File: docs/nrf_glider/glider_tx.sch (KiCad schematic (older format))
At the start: 12 parts

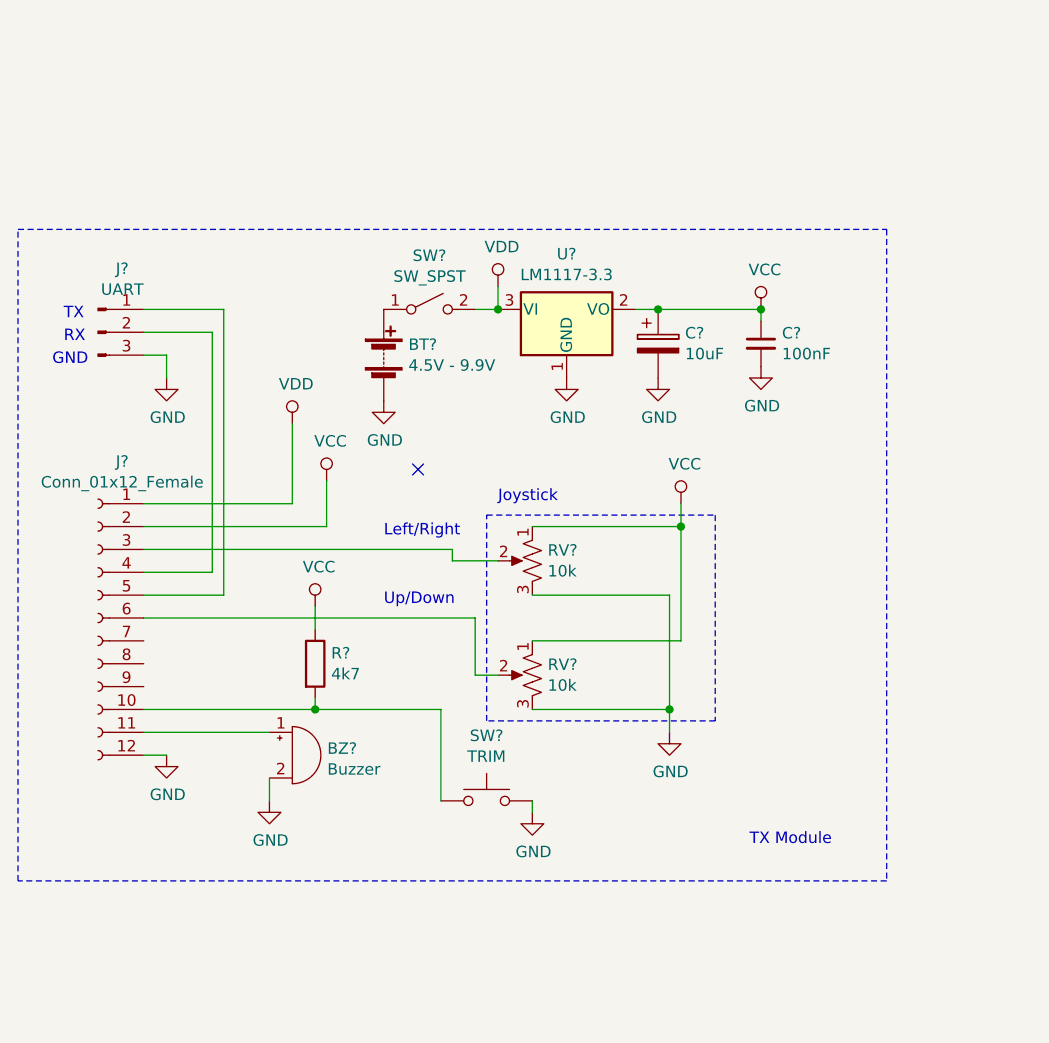
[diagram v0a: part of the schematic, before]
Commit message: added hierarchical sheets and labels
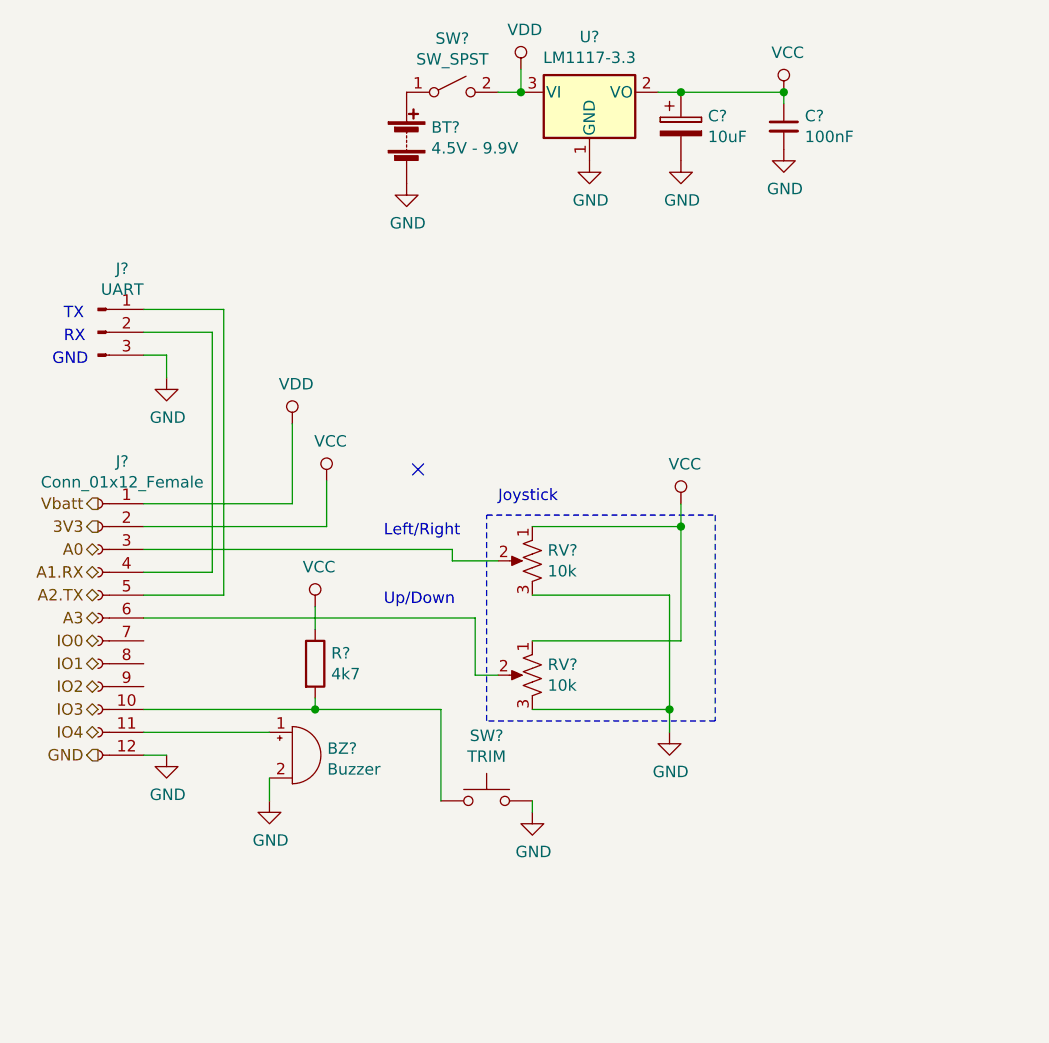
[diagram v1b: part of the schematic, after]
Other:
- note removed: "TX Module"
- moved on the sheet: BT?, C?, SW?, U?
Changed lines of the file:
@@
 $Descr A4 11693 8268
 encoding utf-8
-Sheet 1 4
+Sheet 3 5
 Title ""
 Date ""
@@
 L Regulator_Linear:LM1117-3.3 U?
 U 1 1 5BD2C866
-P 6200 2400
-F 0 "U?" H 6200 2642 50  0000 C CNN
-F 1 "LM1117-3.3" H 6200 2551 50  0000 C CNN
-F 2 "" H 6200 2400 50  0001 C CNN
-F 3 "http://www.ti.com/lit/ds/symlink/lm1117.pdf" H 6200 2400 50  0001 C CNN
-	1    6200 2400
+P 6300 1450
+F 0 "U?" H 6300 1692 50  0000 C CNN
+F 1 "LM1117-3.3" H 6300 1601 50  0000 C CNN
+F 2 "" H 6300 1450 50  0001 C CNN
+F 3 "http://www.ti.com/lit/ds/symlink/lm1117.pdf" H 6300 1450 50  0001 C CNN
+	1    6300 1450
 	1    0    0    -1
 $EndComp
@@
 L power:GND #PWR?
 U 1 1 5BD2C86D
-P 6200 2700
-F 0 "#PWR?" H 6200 2450 50  0001 C CNN
-F 1 "GND" H 6205 2527 50  0000 C CNN
-F 2 "" H 6200 2700 50  0001 C CNN
-F 3 "" H 6200 2700 50  0001 C CNN
-	1    6200 2700
+P 6300 1750
+F 0 "#PWR?" H 6300 1500 50  0001 C CNN
+F 1 "GND" H 6305 1577 50  0000 C CNN
+F 2 "" H 6300 1750 50  0001 C CNN
+F 3 "" H 6300 1750 50  0001 C CNN
+	1    6300 1750
 	1    0    0    -1
 $EndComp
@@
 L Device:Battery BT?
 U 1 1 5BD2C873
-P 5400 2600
-F 0 "BT?" H 5508 2646 50  0000 L CNN
-F 1 "4.5V - 9.9V" H 5508 2555 50  0000 L CNN
-F 2 "Connector_PinHeader_2.54mm:PinHeader_1x02_P2.54mm_Vertical" V 5400 2660 50  0001 C CNN
-F 3 "~" V 5400 2660 50  0001 C CNN
-	1    5400 2600
+P 5500 1650
+F 0 "BT?" H 5608 1696 50  0000 L CNN
+F 1 "4.5V - 9.9V" H 5608 1605 50  0000 L CNN
+F 2 "Connector_PinHeader_2.54mm:PinHeader_1x02_P2.54mm_Vertical" V 5500 1710 50  0001 C CNN
+F 3 "~" V 5500 1710 50  0001 C CNN
+	1    5500 1650
 	1    0    0    -1
 $EndComp
@@
 L power:GND #PWR?
 U 1 1 5BD2C87B
-P 5400 2800
-F 0 "#PWR?" H 5400 2550 50  0001 C CNN
-F 1 "GND" H 5405 2627 50  0000 C CNN
-F 2 "" H 5400 2800 50  0001 C CNN
-F 3 "" H 5400 2800 50  0001 C CNN
-	1    5400 2800
+P 5500 1850
+F 0 "#PWR?" H 5500 1600 50  0001 C CNN
+F 1 "GND" H 5505 1677 50  0000 C CNN
+F 2 "" H 5500 1850 50  0001 C CNN
+F 3 "" H 5500 1850 50  0001 C CNN
+	1    5500 1850
 	1    0    0    -1
 $EndComp
@@
 L power:VCC #PWR?
 U 1 1 5BD2C881
-P 7050 2400
-F 0 "#PWR?" H 7050 2250 50  0001 C CNN
-F 1 "VCC" H 7067 2573 50  0000 C CNN
-F 2 "" H 7050 2400 50  0001 C CNN
-F 3 "" H 7050 2400 50  0001 C CNN
-	1    7050 2400
+P 7150 1450
+F 0 "#PWR?" H 7150 1300 50  0001 C CNN
+F 1 "VCC" H 7167 1623 50  0000 C CNN
+F 2 "" H 7150 1450 50  0001 C CNN
+F 3 "" H 7150 1450 50  0001 C CNN
+	1    7150 1450
 	1    0    0    -1
 $EndComp
@@
 L Device:C_Small C?
 U 1 1 5BD2C887
-P 7050 2550
-F 0 "C?" H 7142 2596 50  0000 L CNN
-F 1 "100nF" H 7142 2505 50  0000 L CNN
-F 2 "Capacitor_THT:C_Disc_D5.0mm_W2.5mm_P5.00mm" H 7050 2550 50  0001 C CNN
-F 3 "~" H 7050 2550 50  0001 C CNN
-	1    7050 2550
+P 7150 1600
+F 0 "C?" H 7242 1646 50  0000 L CNN
+F 1 "100nF" H 7242 1555 50  0000 L CNN
+F 2 "Capacitor_THT:C_Disc_D5.0mm_W2.5mm_P5.00mm" H 7150 1600 50  0001 C CNN
+F 3 "~" H 7150 1600 50  0001 C CNN
+	1    7150 1600
 	1    0    0    -1
 $EndComp
@@
 L Device:CP C?
 U 1 1 5BD2C88E
-P 6600 2550
-F 0 "C?" H 6718 2596 50  0000 L CNN
-F 1 "10uF" H 6718 2505 50  0000 L CNN
-F 2 "Capacitor_THT:CP_Radial_D8.0mm_P2.50mm" H 6638 2400 50  0001 C CNN
-F 3 "~" H 6600 2550 50  0001 C CNN
-	1    6600 2550
+P 6700 1600
+F 0 "C?" H 6818 1646 50  0000 L CNN
+F 1 "10uF" H 6818 1555 50  0000 L CNN
+F 2 "Capacitor_THT:CP_Radial_D8.0mm_P2.50mm" H 6738 1450 50  0001 C CNN
+F 3 "~" H 6700 1600 50  0001 C CNN
+	1    6700 1600
 	1    0    0    -1
 $EndComp
@@
 L power:GND #PWR?
 U 1 1 5BD2C895
-P 6600 2700
-F 0 "#PWR?" H 6600 2450 50  0001 C CNN
-F 1 "GND" H 6605 2527 50  0000 C CNN
-F 2 "" H 6600 2700 50  0001 C CNN
-F 3 "" H 6600 2700 50  0001 C CNN
-	1    6600 2700
+P 6700 1750
+F 0 "#PWR?" H 6700 1500 50  0001 C CNN
+F 1 "GND" H 6705 1577 50  0000 C CNN
+F 2 "" H 6700 1750 50  0001 C CNN
+F 3 "" H 6700 1750 50  0001 C CNN
+	1    6700 1750
 	1    0    0    -1
 $EndComp
@@
 L power:GND #PWR?
 U 1 1 5BD2C89B
-P 7050 2650
-F 0 "#PWR?" H 7050 2400 50  0001 C CNN
-F 1 "GND" H 7055 2477 50  0000 C CNN
-F 2 "" H 7050 2650 50  0001 C CNN
-F 3 "" H 7050 2650 50  0001 C CNN
-	1    7050 2650
-	1    0    0    -1
-$EndComp
-Wire Wire Line
-	6500 2400 6600 2400
+P 7150 1700
+F 0 "#PWR?" H 7150 1450 50  0001 C CNN
+F 1 "GND" H 7155 1527 50  0000 C CNN
+F 2 "" H 7150 1700 50  0001 C CNN
+F 3 "" H 7150 1700 50  0001 C CNN
+	1    7150 1700
+	1    0    0    -1
+$EndComp
+Wire Wire Line
+	6600 1450 6700 1450
 $Comp
 L power:VDD #PWR?
 U 1 1 5BD2C8A2
-P 5900 2300
-F 0 "#PWR?" H 5900 2150 50  0001 C CNN
-F 1 "VDD" H 5917 2473 50  0000 C CNN
-F 2 "" H 5900 2300 50  0001 C CNN
-F 3 "" H 5900 2300 50  0001 C CNN
-	1    5900 2300
-	1    0    0    -1
-$EndComp
-Wire Wire Line
-	7050 2400 7050 2450
-Connection ~ 7050 2400
-Wire Wire Line
-	6600 2400 7050 2400
-Connection ~ 6600 2400
-Wire Notes Line
-	3800 2050 7600 2050
-Wire Notes Line
-	7600 2050 7600 4900
-Wire Notes Line
-	7600 4900 3800 4900
-Wire Notes Line
-	3800 4900 3800 2050
-Text Notes 7000 4750 0    50   ~ 0
-TX Module
+P 6000 1350
+F 0 "#PWR?" H 6000 1200 50  0001 C CNN
+F 1 "VDD" H 6017 1523 50  0000 C CNN
+F 2 "" H 6000 1350 50  0001 C CNN
+F 3 "" H 6000 1350 50  0001 C CNN
+	1    6000 1350
+	1    0    0    -1
+$EndComp
+Wire Wire Line
+	7150 1450 7150 1500
+Connection ~ 7150 1450
+Wire Wire Line
+	6700 1450 7150 1450
+Connection ~ 6700 1450
 Wire Wire Line
 	4350 4250 4900 4250
@@
 L Switch:SW_SPST SW?
 U 1 1 5BD0D3D1
-P 5600 2400
-F 0 "SW?" H 5600 2635 50  0000 C CNN
-F 1 "SW_SPST" H 5600 2544 50  0000 C CNN
-F 2 "" H 5600 2400 50  0001 C CNN
-F 3 "" H 5600 2400 50  0001 C CNN
-	1    5600 2400
-	1    0    0    -1
-$EndComp
-Wire Wire Line
-	5800 2400 5900 2400
-Wire Wire Line
-	5900 2300 5900 2400
-Connection ~ 5900 2400
+P 5700 1450
+F 0 "SW?" H 5700 1685 50  0000 C CNN
+F 1 "SW_SPST" H 5700 1594 50  0000 C CNN
+F 2 "" H 5700 1450 50  0001 C CNN
+F 3 "" H 5700 1450 50  0001 C CNN
+	1    5700 1450
+	1    0    0    -1
+$EndComp
+Wire Wire Line
+	5900 1450 6000 1450
+Wire Wire Line
+	6000 1350 6000 1450
+Connection ~ 6000 1450
+Text HLabel 4150 3250 0    50   Output ~ 0
+Vbatt
+Text HLabel 4150 3350 0    50   Output ~ 0
+3V3
+Text HLabel 4150 3450 0    50   BiDi ~ 0
+A0
+Text HLabel 4150 3550 0    50   BiDi ~ 0
+A1.RX
+Text HLabel 4150 3650 0    50   BiDi ~ 0
+A2.TX
+Text HLabel 4150 3750 0    50   BiDi ~ 0
+A3
+Text HLabel 4150 3850 0    50   BiDi ~ 0
+IO0
+Text HLabel 4150 3950 0    50   BiDi ~ 0
+IO1
+Text HLabel 4150 4050 0    50   BiDi ~ 0
+IO2
+Text HLabel 4150 4150 0    50   BiDi ~ 0
+IO3
+Text HLabel 4150 4250 0    50   BiDi ~ 0
+IO4
+Text HLabel 4150 4350 0    50   Output ~ 0
+GND
 $EndSCHEMATC

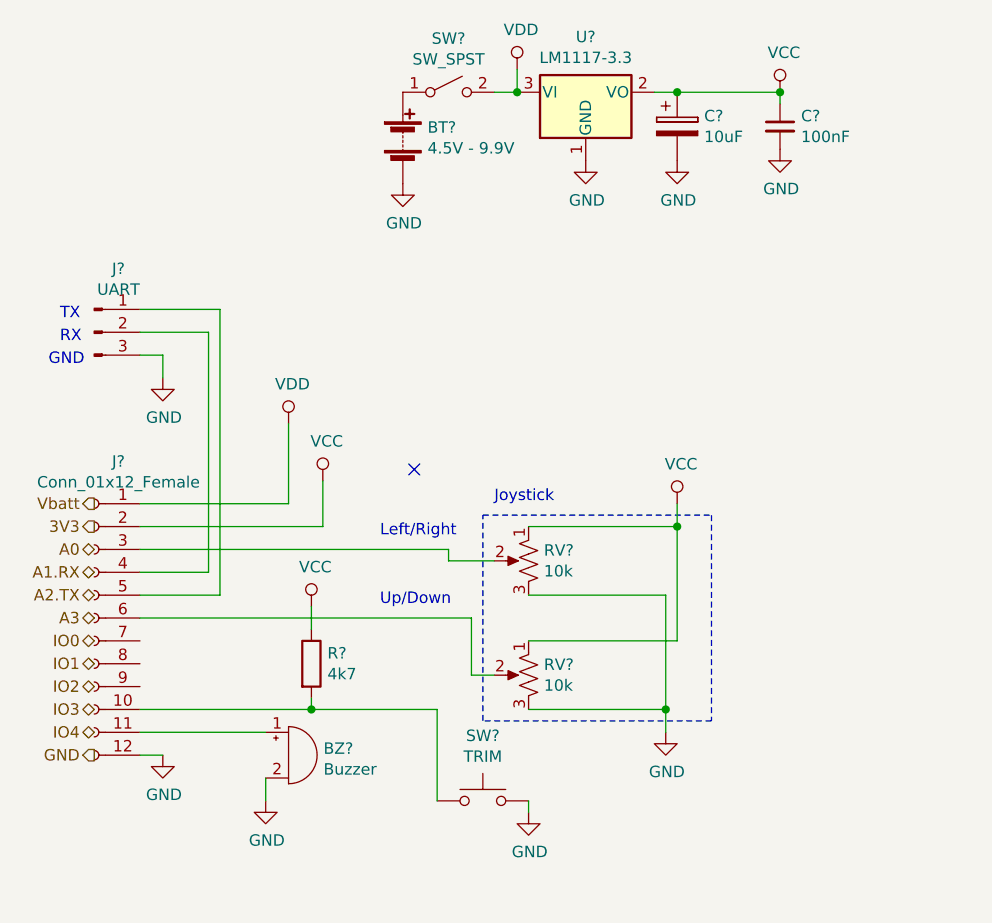
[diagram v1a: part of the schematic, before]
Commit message: remove and ignore bak files
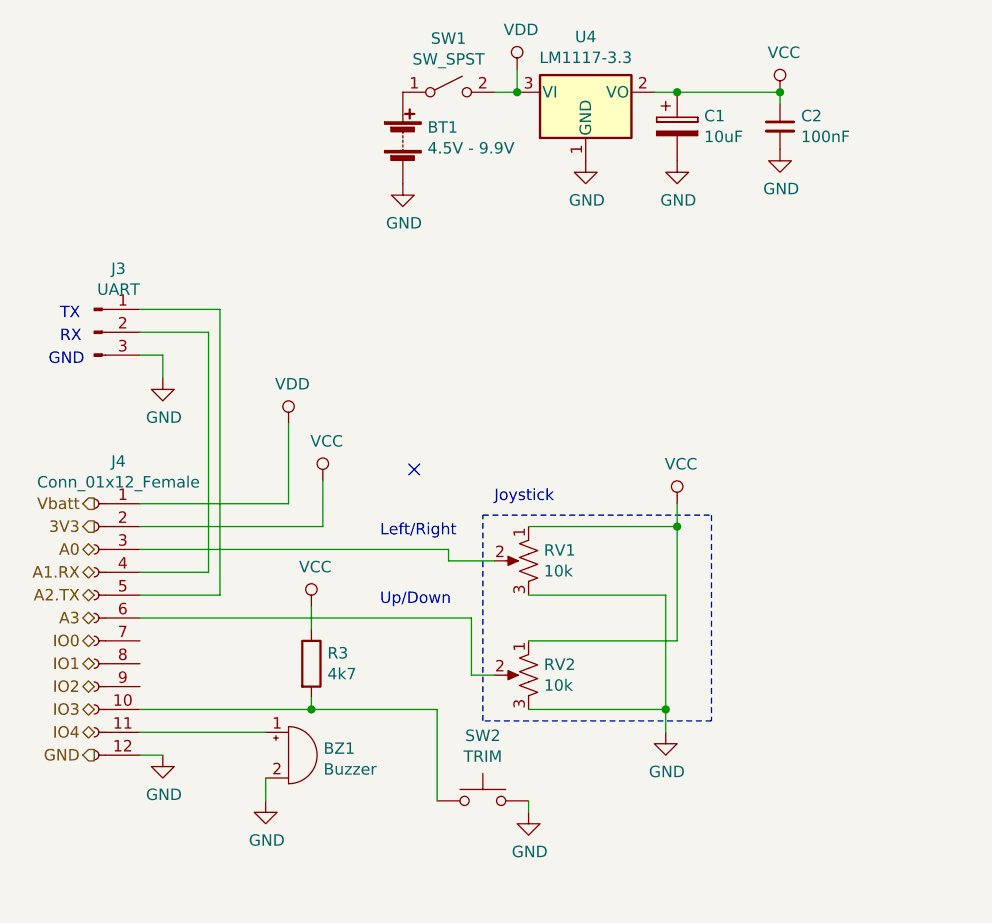
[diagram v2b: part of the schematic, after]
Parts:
- gave numbers to parts that had none: 12
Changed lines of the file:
@@
 $EndDescr
 $Comp
-L Connector:Conn_01x12_Female J?
+L Connector:Conn_01x12_Female J4
 U 1 1 5BD138DF
 P 4150 3750
-F 0 "J?" H 4044 4435 50  0000 C CNN
+F 0 "J4" H 4044 4435 50  0000 C CNN
 F 1 "Conn_01x12_Female" H 4044 4344 50  0000 C CNN
 F 2 "Connector_PinHeader_2.54mm:PinHeader_1x12_P2.54mm_Vertical" H 4150 3750 50  0001 C CNN
@@
 $EndComp
 $Comp
-L power:VCC #PWR?
+L power:VCC #PWR0114
 U 1 1 5BD1D3CE
 P 5150 3150
-F 0 "#PWR?" H 5150 3000 50  0001 C CNN
+F 0 "#PWR0114" H 5150 3000 50  0001 C CNN
 F 1 "VCC" H 5167 3323 50  0000 C CNN
 F 2 "" H 5150 3150 50  0001 C CNN
@@
 $EndComp
 $Comp
-L power:VDD #PWR?
+L power:VDD #PWR0115
 U 1 1 5BD1D429
 P 5000 2900
-F 0 "#PWR?" H 5000 2750 50  0001 C CNN
+F 0 "#PWR0115" H 5000 2750 50  0001 C CNN
 F 1 "VDD" H 5017 3073 50  0000 C CNN
 F 2 "" H 5000 2900 50  0001 C CNN
@@
 $EndComp
 $Comp
-L power:GND #PWR?
+L power:GND #PWR0116
 U 1 1 5BD1F482
 P 4450 4350
-F 0 "#PWR?" H 4450 4100 50  0001 C CNN
+F 0 "#PWR0116" H 4450 4100 50  0001 C CNN
 F 1 "GND" H 4455 4177 50  0000 C CNN
 F 2 "" H 4450 4350 50  0001 C CNN
@@
 NoConn ~ 5550 3100
 $Comp
-L Device:R_POT_US RV?
+L Device:R_POT_US RV1
 U 1 1 5BD2C04D
 P 6050 3500
-F 0 "RV?" H 5983 3546 50  0000 R CNN
+F 0 "RV1" H 5983 3546 50  0000 R CNN
 F 1 "10k" H 5983 3455 50  0000 R CNN
 F 2 "Potentiometer_THT:Potentiometer_ACP_CA9-V10_Vertical" H 6050 3500 50  0001 C CNN
@@
 $EndComp
 $Comp
-L Device:R_POT_US RV?
+L Device:R_POT_US RV2
 U 1 1 5BD2C0E7
 P 6050 4000
-F 0 "RV?" H 5983 4046 50  0000 R CNN
+F 0 "RV2" H 5983 4046 50  0000 R CNN
 F 1 "10k" H 5983 3955 50  0000 R CNN
 F 2 "Potentiometer_THT:Potentiometer_ACP_CA9-V10_Vertical" H 6050 4000 50  0001 C CNN
@@
 $EndComp
 $Comp
-L Device:Buzzer BZ?
+L Device:Buzzer BZ1
 U 1 1 5BD2C1D8
 P 5000 4350
-F 0 "BZ?" H 5153 4379 50  0000 L CNN
+F 0 "BZ1" H 5153 4379 50  0000 L CNN
 F 1 "Buzzer" H 5153 4288 50  0000 L CNN
 F 2 "Buzzer_Beeper:Buzzer_15x7.5RM7.6" V 4975 4450 50  0001 C CNN
@@
 $EndComp
 $Comp
-L Switch:SW_Push SW?
+L Switch:SW_Push SW2
 U 1 1 5BD2C33F
 P 5850 4550
-F 0 "SW?" H 5850 4835 50  0000 C CNN
+F 0 "SW2" H 5850 4835 50  0000 C CNN
 F 1 "TRIM" H 5850 4744 50  0000 C CNN
 F 2 "Button_Switch_THT:SW_PUSH_6mm_H5mm" H 5850 4750 50  0001 C CNN
@@
 $EndComp
 $Comp
-L Regulator_Linear:LM1117-3.3 U?
+L Regulator_Linear:LM1117-3.3 U4
 U 1 1 5BD2C866
 P 6300 1450
-F 0 "U?" H 6300 1692 50  0000 C CNN
+F 0 "U4" H 6300 1692 50  0000 C CNN
 F 1 "LM1117-3.3" H 6300 1601 50  0000 C CNN
 F 2 "" H 6300 1450 50  0001 C CNN
@@
 $EndComp
 $Comp
-L power:GND #PWR?
+L power:GND #PWR0117
 U 1 1 5BD2C86D
 P 6300 1750
-F 0 "#PWR?" H 6300 1500 50  0001 C CNN
+F 0 "#PWR0117" H 6300 1500 50  0001 C CNN
 F 1 "GND" H 6305 1577 50  0000 C CNN
 F 2 "" H 6300 1750 50  0001 C CNN
@@
 $EndComp
 $Comp
-L Device:Battery BT?
+L Device:Battery BT1
 U 1 1 5BD2C873
 P 5500 1650
-F 0 "BT?" H 5608 1696 50  0000 L CNN
+F 0 "BT1" H 5608 1696 50  0000 L CNN
 F 1 "4.5V - 9.9V" H 5608 1605 50  0000 L CNN
 F 2 "Connector_PinHeader_2.54mm:PinHeader_1x02_P2.54mm_Vertical" V 5500 1710 50  0001 C CNN
@@
 $EndComp
 $Comp
-L power:GND #PWR?
+L power:GND #PWR0118
 U 1 1 5BD2C87B
 P 5500 1850
-F 0 "#PWR?" H 5500 1600 50  0001 C CNN
+F 0 "#PWR0118" H 5500 1600 50  0001 C CNN
 F 1 "GND" H 5505 1677 50  0000 C CNN
 F 2 "" H 5500 1850 50  0001 C CNN
@@
 $EndComp
 $Comp
-L power:VCC #PWR?
+L power:VCC #PWR0119
 U 1 1 5BD2C881
 P 7150 1450
-F 0 "#PWR?" H 7150 1300 50  0001 C CNN
+F 0 "#PWR0119" H 7150 1300 50  0001 C CNN
 F 1 "VCC" H 7167 1623 50  0000 C CNN
 F 2 "" H 7150 1450 50  0001 C CNN
@@
 $EndComp
 $Comp
-L Device:C_Small C?
+L Device:C_Small C2
 U 1 1 5BD2C887
 P 7150 1600
-F 0 "C?" H 7242 1646 50  0000 L CNN
+F 0 "C2" H 7242 1646 50  0000 L CNN
 F 1 "100nF" H 7242 1555 50  0000 L CNN
 F 2 "Capacitor_THT:C_Disc_D5.0mm_W2.5mm_P5.00mm" H 7150 1600 50  0001 C CNN
@@
 $EndComp
 $Comp
-L Device:CP C?
+L Device:CP C1
 U 1 1 5BD2C88E
 P 6700 1600
-F 0 "C?" H 6818 1646 50  0000 L CNN
+F 0 "C1" H 6818 1646 50  0000 L CNN
 F 1 "10uF" H 6818 1555 50  0000 L CNN
 F 2 "Capacitor_THT:CP_Radial_D8.0mm_P2.50mm" H 6738 1450 50  0001 C CNN
@@
 $EndComp
 $Comp
-L power:GND #PWR?
+L power:GND #PWR0120
 U 1 1 5BD2C895
 P 6700 1750
-F 0 "#PWR?" H 6700 1500 50  0001 C CNN
+F 0 "#PWR0120" H 6700 1500 50  0001 C CNN
 F 1 "GND" H 6705 1577 50  0000 C CNN
 F 2 "" H 6700 1750 50  0001 C CNN
@@
 $EndComp
 $Comp
-L power:GND #PWR?
+L power:GND #PWR0121
 U 1 1 5BD2C89B
 P 7150 1700
-F 0 "#PWR?" H 7150 1450 50  0001 C CNN
+F 0 "#PWR0121" H 7150 1450 50  0001 C CNN
 F 1 "GND" H 7155 1527 50  0000 C CNN
 F 2 "" H 7150 1700 50  0001 C CNN
@@
 	6600 1450 6700 1450
 $Comp
-L power:VDD #PWR?
+L power:VDD #PWR0122
 U 1 1 5BD2C8A2
 P 6000 1350
-F 0 "#PWR?" H 6000 1200 50  0001 C CNN
+F 0 "#PWR0122" H 6000 1200 50  0001 C CNN
 F 1 "VDD" H 6017 1523 50  0000 C CNN
 F 2 "" H 6000 1350 50  0001 C CNN
@@
 	4350 4250 4900 4250
 $Comp
-L power:GND #PWR?
+L power:GND #PWR0123
 U 1 1 5BD90917
 P 4900 4550
-F 0 "#PWR?" H 4900 4300 50  0001 C CNN
+F 0 "#PWR0123" H 4900 4300 50  0001 C CNN
 F 1 "GND" H 4905 4377 50  0000 C CNN
 F 2 "" H 4900 4550 50  0001 C CNN
@@
 	5800 4000 5900 4000
 $Comp
-L power:VCC #PWR?
+L power:VCC #PWR0124
 U 1 1 5BDA8B66
 P 6700 3250
-F 0 "#PWR?" H 6700 3100 50  0001 C CNN
+F 0 "#PWR0124" H 6700 3100 50  0001 C CNN
 F 1 "VCC" H 6717 3423 50  0000 C CNN
 F 2 "" H 6700 3250 50  0001 C CNN
@@
 Connection ~ 6700 3350
 $Comp
-L power:GND #PWR?
+L power:GND #PWR0125
 U 1 1 5BDB1721
 P 6650 4250
-F 0 "#PWR?" H 6650 4000 50  0001 C CNN
+F 0 "#PWR0125" H 6650 4000 50  0001 C CNN
 F 1 "GND" H 6655 4077 50  0000 C CNN
 F 2 "" H 6650 4250 50  0001 C CNN
@@
 Connection ~ 6650 4150
 $Comp
-L power:GND #PWR?
+L power:GND #PWR0126
 U 1 1 5BDC42C6
 P 6050 4600
-F 0 "#PWR?" H 6050 4350 50  0001 C CNN
+F 0 "#PWR0126" H 6050 4350 50  0001 C CNN
 F 1 "GND" H 6055 4427 50  0000 C CNN
 F 2 "" H 6050 4600 50  0001 C CNN
@@
 	5650 4150 5650 4550
 $Comp
-L Device:R R?
+L Device:R R3
 U 1 1 5BDCDB06
 P 5100 3950
-F 0 "R?" H 5170 3996 50  0000 L CNN
+F 0 "R3" H 5170 3996 50  0000 L CNN
 F 1 "4k7" H 5170 3905 50  0000 L CNN
 F 2 "Resistor_THT:R_Axial_DIN0411_L9.9mm_D3.6mm_P12.70mm_Horizontal" V 5030 3950 50  0001 C CNN
@@
 $EndComp
 $Comp
-L power:VCC #PWR?
+L power:VCC #PWR0127
 U 1 1 5BDCDC3B
 P 5100 3700
-F 0 "#PWR?" H 5100 3550 50  0001 C CNN
+F 0 "#PWR0127" H 5100 3550 50  0001 C CNN
 F 1 "VCC" H 5117 3873 50  0000 C CNN
 F 2 "" H 5100 3700 50  0001 C CNN
@@
 $EndComp
 $Comp
-L Connector:Conn_01x03_Male J?
+L Connector:Conn_01x03_Male J3
 U 1 1 5BCF8F2B
 P 4150 2500
-F 0 "J?" H 4256 2778 50  0000 C CNN
+F 0 "J3" H 4256 2778 50  0000 C CNN
 F 1 "UART" H 4256 2687 50  0000 C CNN
 F 2 "Connector_PinHeader_2.54mm:PinHeader_1x03_P2.54mm_Horizontal" H 4150 2500 50  0001 C CNN
@@
 	4700 3650 4350 3650
 $Comp
-L power:GND #PWR?
+L power:GND #PWR0128
 U 1 1 5BD038ED
 P 4450 2700
-F 0 "#PWR?" H 4450 2450 50  0001 C CNN
+F 0 "#PWR0128" H 4450 2450 50  0001 C CNN
 F 1 "GND" H 4455 2527 50  0000 C CNN
 F 2 "" H 4450 2700 50  0001 C CNN
@@
 created by Toby Kurien
 $Comp
-L Switch:SW_SPST SW?
+L Switch:SW_SPST SW1
 U 1 1 5BD0D3D1
 P 5700 1450
-F 0 "SW?" H 5700 1685 50  0000 C CNN
+F 0 "SW1" H 5700 1685 50  0000 C CNN
 F 1 "SW_SPST" H 5700 1594 50  0000 C CNN
 F 2 "" H 5700 1450 50  0001 C CNN
